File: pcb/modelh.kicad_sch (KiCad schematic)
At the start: 45 parts, among them J1 USB_C_Receptacle_USB2.0, J2 Conn_01x16, J3 Conn_01x12, J4 Conn_01x04, J5 Conn_02x03_Odd_Even, J6 Conn_02x05_Odd_Even, J7 Conn_01x05, J8 Conn_01x05, J9 Conn_01x05, SW1 SW_Push, U1 STM32F103C8Tx, U2 AMS1117-3.3, Y1 8MHz

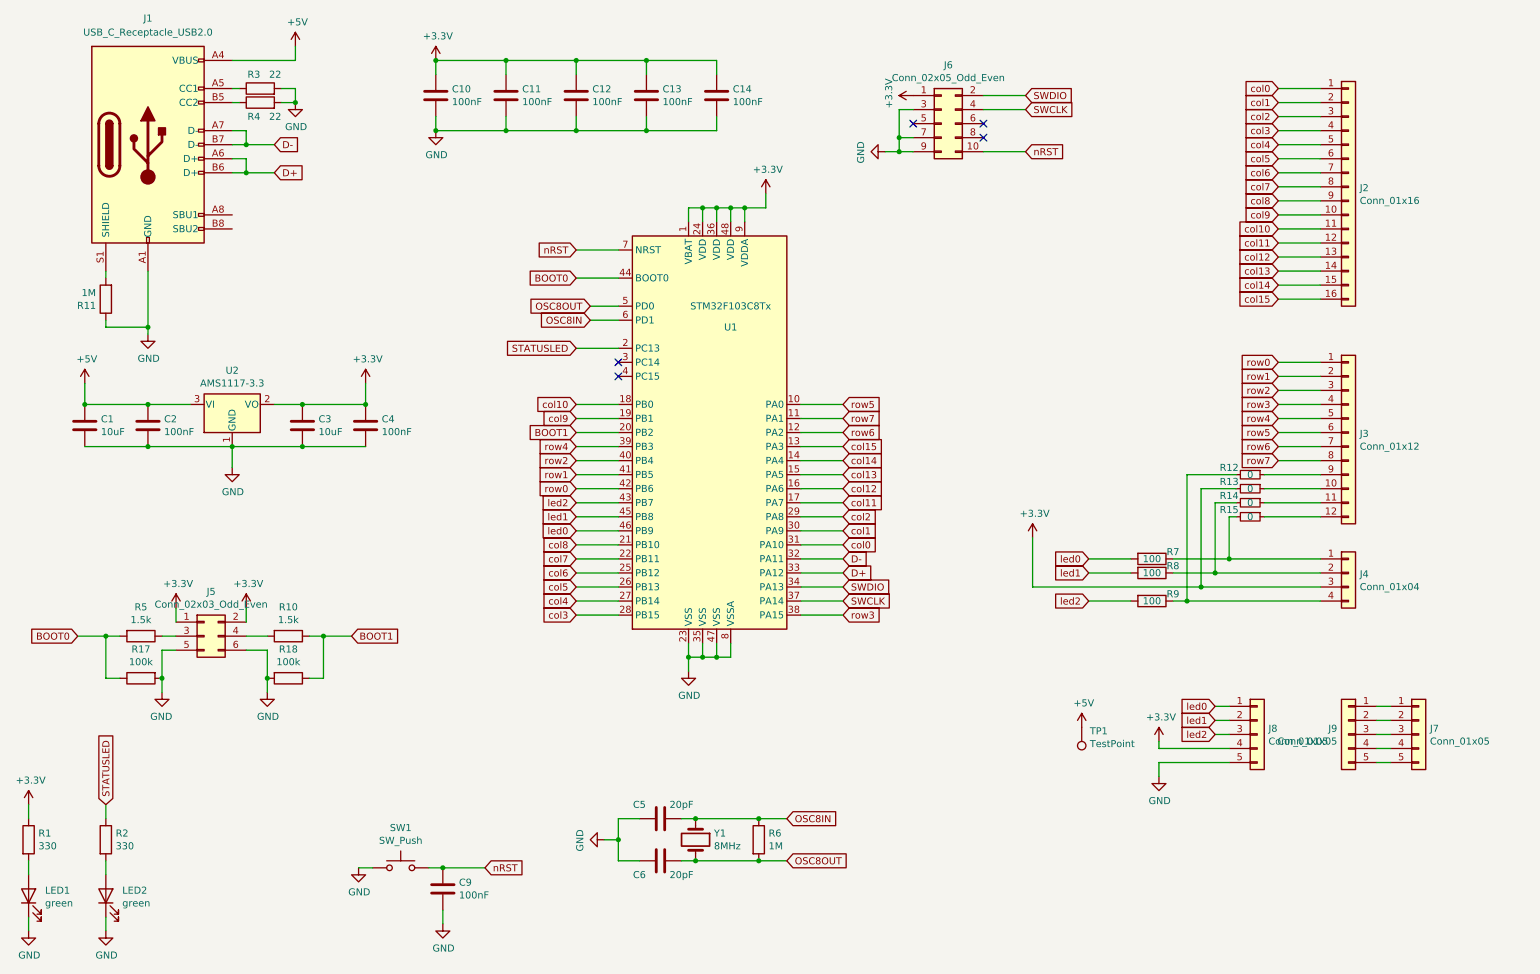
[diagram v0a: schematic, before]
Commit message: Renames a few components
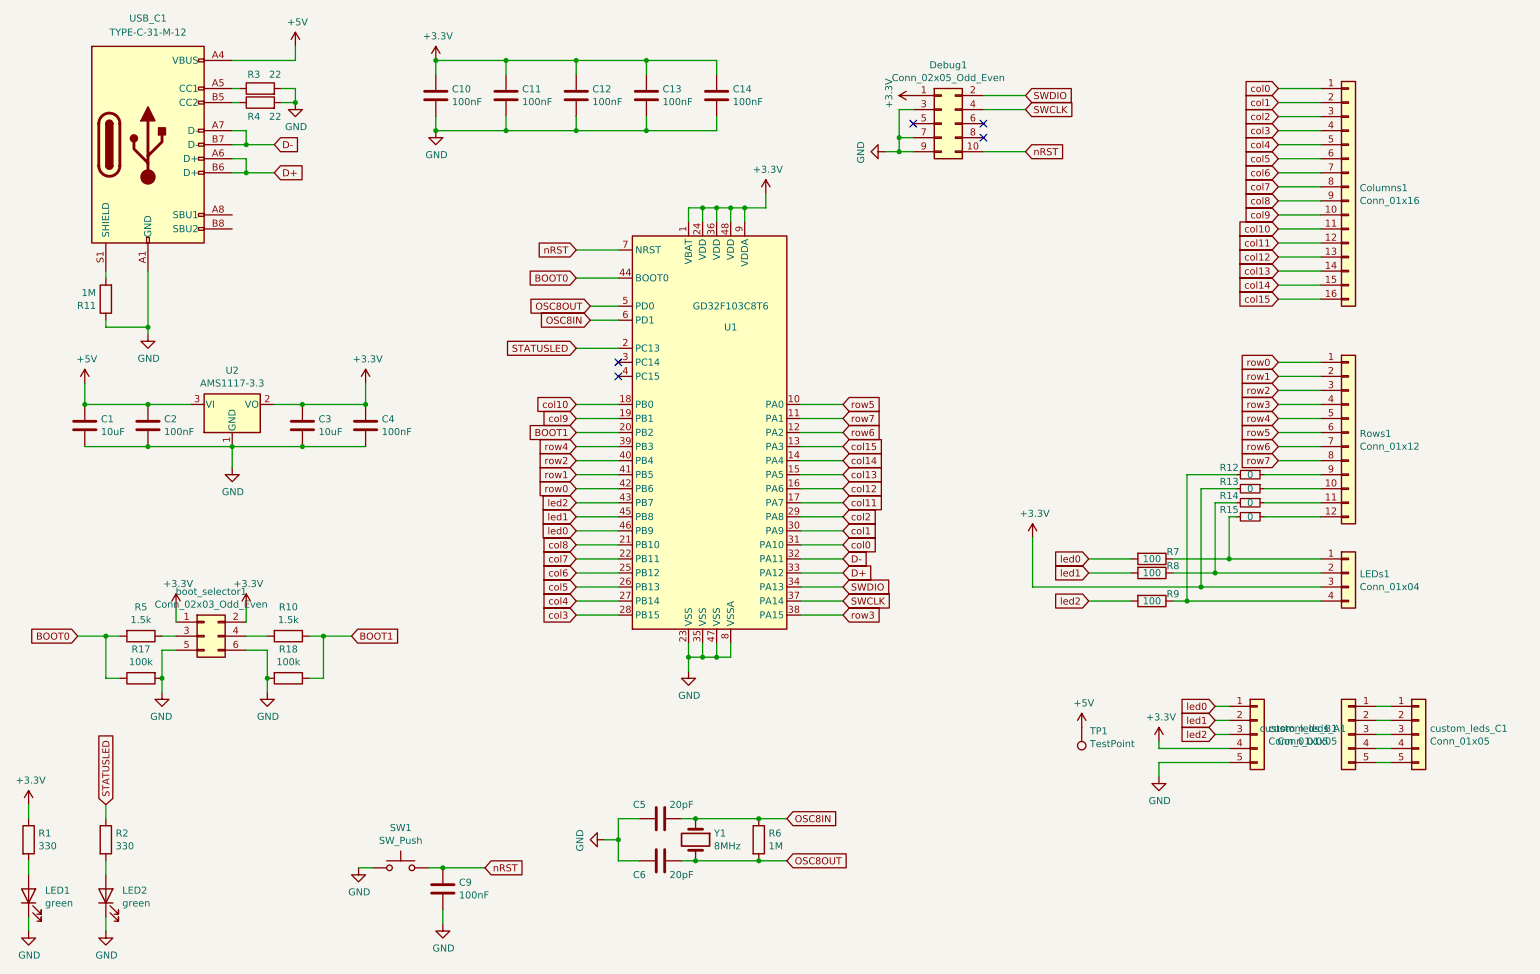
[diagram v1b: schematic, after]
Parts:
- R11: LCSC C22843 -> C269433
- U1: value STM32F103C8Tx -> GD32F103C8T6; LCSC C8734 -> C77994
- USB_C1: renamed from J1; value USB_C_Receptacle_USB2.0 -> TYPE-C-31-M-12; LCSC (none) -> C165948
- renumbered J2 to Columns1, J6 to Debug1, J4 to LEDs1, J3 to Rows1, J5 to boot_selector1, J8 to custom_leds_A1, J9 to custom_leds_B1, J7 to custom_leds_C1
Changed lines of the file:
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@@
   (symbol (lib_id "Connector_Generic:Conn_01x16") (at 261.62 49.53 0) (unit 1)
     (in_bom yes) (on_board yes)
-    (property "Reference" "J2" (id 0) (at 263.652 49.7332 0)
+    (property "Reference" "Columns1" (id 0) (at 263.652 49.7332 0)
       (effects (font (size 1.27 1.27)) (justify left))
     )
@@
   (symbol (lib_id "Connector_Generic:Conn_01x04") (at 261.62 119.38 0) (unit 1)
     (in_bom yes) (on_board yes)
-    (property "Reference" "J4" (id 0) (at 263.652 119.5832 0)
+    (property "Reference" "LEDs1" (id 0) (at 263.652 119.5832 0)
       (effects (font (size 1.27 1.27)) (justify left))
     )
@@
     (in_bom yes) (on_board yes)
     (property "Reference" "U1" (id 0) (at 149.86 74.93 0))
-    (property "Value" "STM32F103C8Tx" (id 1) (at 149.86 71.12 0))
+    (property "Value" "GD32F103C8T6" (id 1) (at 149.86 71.12 0))
     (property "Footprint" "Package_QFP:LQFP-48_7x7mm_P0.5mm" (id 2) (at 132.08 129.54 0)
       (effects (font (size 1.27 1.27)) (justify right) hide)
     )
-    (property "Datasheet" "http://www.st.com/st-web-ui/static/active/en/resource/technical/document/datasheet/CD00161566.pdf" (id 3) (at 147.32 93.98 0)
-      (effects (font (size 1.27 1.27)) hide)
-    )
-    (property "LCSC" "C8734" (id 4) (at 147.32 93.98 0)
+    (property "Datasheet" "https://datasheet.lcsc.com/lcsc/1809201023_GigaDevice-Semicon-Beijing-GD32F103C8T6_C77994.pdf" (id 3) (at 147.32 93.98 0)
+      (effects (font (size 1.27 1.27)) hide)
+    )
+    (property "LCSC" "C77994" (id 4) (at 147.32 93.98 0)
       (effects (font (size 1.27 1.27)) hide)
     )
@@
   (symbol (lib_id "Connector_Generic:Conn_02x05_Odd_Even") (at 187.96 38.1 0) (unit 1)
     (in_bom yes) (on_board yes)
-    (property "Reference" "J6" (id 0) (at 189.23 27.5082 0))
+    (property "Reference" "Debug1" (id 0) (at 189.23 27.5082 0))
     (property "Value" "Conn_02x05_Odd_Even" (id 1) (at 189.23 29.8196 0))
     (property "Footprint" "Connector_IDC:IDC-Header_2x05_P2.54mm_Vertical" (id 2) (at 187.96 38.1 0)
@@
   (symbol (lib_id "Connector_Generic:Conn_01x05") (at 274.32 148.59 0) (unit 1)
     (in_bom yes) (on_board yes)
-    (property "Reference" "J7" (id 0) (at 276.352 147.5232 0)
+    (property "Reference" "custom_leds_C1" (id 0) (at 276.352 147.5232 0)
       (effects (font (size 1.27 1.27)) (justify left))
     )
@@
   (symbol (lib_id "Connector_Generic:Conn_01x05") (at 245.11 148.59 0) (unit 1)
     (in_bom yes) (on_board yes)
-    (property "Reference" "J8" (id 0) (at 247.142 147.5232 0)
+    (property "Reference" "custom_leds_A1" (id 0) (at 247.142 147.5232 0)
       (effects (font (size 1.27 1.27)) (justify left))
     )
@@
   (symbol (lib_id "Connector_Generic:Conn_01x05") (at 261.62 148.59 0) (mirror y) (unit 1)
     (in_bom yes) (on_board yes)
-    (property "Reference" "J9" (id 0) (at 259.588 147.5232 0)
+    (property "Reference" "custom_leds_B1" (id 0) (at 259.588 147.5232 0)
       (effects (font (size 1.27 1.27)) (justify left))
     )
@@
       (effects (font (size 1.27 1.27)) hide)
     )
-    (property "LCSC" "C22843" (id 4) (at 36.83 69.85 0)
+    (property "LCSC" "C269433" (id 4) (at 36.83 69.85 0)
       (effects (font (size 1.27 1.27)) hide)
     )
@@
   (symbol (lib_id "Connector_Generic:Conn_02x03_Odd_Even") (at 54.61 130.81 0) (unit 1)
     (in_bom yes) (on_board yes)
-    (property "Reference" "J5" (id 0) (at 55.88 122.7582 0))
+    (property "Reference" "boot_selector1" (id 0) (at 55.88 122.7582 0))
     (property "Value" "Conn_02x03_Odd_Even" (id 1) (at 55.88 125.0696 0))
     (property "Footprint" "Connector_PinHeader_2.54mm:PinHeader_2x03_P2.54mm_Vertical" (id 2) (at 54.61 130.81 0)
@@
   (symbol (lib_id "Connector_Generic:Conn_01x12") (at 261.62 93.98 0) (unit 1)
     (in_bom yes) (on_board yes)
-    (property "Reference" "J3" (id 0) (at 263.652 94.1832 0)
+    (property "Reference" "Rows1" (id 0) (at 263.652 94.1832 0)
       (effects (font (size 1.27 1.27)) (justify left))
     )
@@
   (symbol (lib_id "Connector:USB_C_Receptacle_USB2.0") (at 44.45 41.91 0) (unit 1)
     (in_bom yes) (on_board yes) (fields_autoplaced)
-    (property "Reference" "J1" (id 0) (at 44.45 19.05 0))
-    (property "Value" "USB_C_Receptacle_USB2.0" (id 1) (at 44.45 21.59 0))
+    (property "Reference" "USB_C1" (id 0) (at 44.45 19.05 0))
+    (property "Value" "TYPE-C-31-M-12" (id 1) (at 44.45 21.59 0))
     (property "Footprint" "Connector_USB:USB_C_Receptacle_HRO_TYPE-C-31-M-12" (id 2) (at 48.26 41.91 0)
       (effects (font (size 1.27 1.27)) hide)
     )
     (property "Datasheet" "https://www.usb.org/sites/default/files/documents/usb_type-c.zip" (id 3) (at 48.26 41.91 0)
+      (effects (font (size 1.27 1.27)) hide)
+    )
+    (property "LCSC" "C165948" (id 4) (at 44.45 41.91 0)
       (effects (font (size 1.27 1.27)) hide)
     )
@@
       (reference "C14") (unit 1) (value "100nF") (footprint "Capacitor_SMD:C_0402_1005Metric")
     )
-    (path "/77142229-b825-44a9-8ee1-1a9eb237340e"
-      (reference "J1") (unit 1) (value "USB_C_Receptacle_USB2.0") (footprint "Connector_USB:USB_C_Receptacle_HRO_TYPE-C-31-M-12")
-    )
     (path "/00000000-0000-0000-0000-00005e88f7ea"
-      (reference "J2") (unit 1) (value "Conn_01x16") (footprint "modelh:ModelH-triomate-cols16")
-    )
-    (path "/00000000-0000-0000-0000-00005f673091"
-      (reference "J3") (unit 1) (value "Conn_01x12") (footprint "modelh:ModelH-triomate-rows12")
-    )
-    (path "/00000000-0000-0000-0000-00005e891730"
-      (reference "J4") (unit 1) (value "Conn_01x04") (footprint "modelh:ModelH-tripmate-leds4")
-    )
-    (path "/00000000-0000-0000-0000-00005f50a2de"
-      (reference "J5") (unit 1) (value "Conn_02x03_Odd_Even") (footprint "Connector_PinHeader_2.54mm:PinHeader_2x03_P2.54mm_Vertical")
+      (reference "Columns1") (unit 1) (value "Conn_01x16") (footprint "modelh:ModelH-triomate-cols16")
     )
     (path "/00000000-0000-0000-0000-00005f0cf1af"
-      (reference "J6") (unit 1) (value "Conn_02x05_Odd_Even") (footprint "Connector_IDC:IDC-Header_2x05_P2.54mm_Vertical")
-    )
-    (path "/00000000-0000-0000-0000-00005f225882"
-      (reference "J7") (unit 1) (value "Conn_01x05") (footprint "Connector_PinSocket_2.54mm:PinSocket_1x05_P2.54mm_Vertical")
-    )
-    (path "/00000000-0000-0000-0000-00005f2b29ec"
-      (reference "J8") (unit 1) (value "Conn_01x05") (footprint "Connector_PinSocket_2.54mm:PinSocket_1x05_P2.54mm_Vertical")
-    )
-    (path "/00000000-0000-0000-0000-00005f2c10c8"
-      (reference "J9") (unit 1) (value "Conn_01x05") (footprint "Connector_PinSocket_2.54mm:PinSocket_1x05_P2.54mm_Vertical")
+      (reference "Debug1") (unit 1) (value "Conn_02x05_Odd_Even") (footprint "Connector_IDC:IDC-Header_2x05_P2.54mm_Vertical")
     )
     (path "/00000000-0000-0000-0000-00005ecc1b17"
@@
       (reference "LED2") (unit 1) (value "green") (footprint "LED_SMD:LED_0805_2012Metric")
     )
+    (path "/00000000-0000-0000-0000-00005e891730"
+      (reference "LEDs1") (unit 1) (value "Conn_01x04") (footprint "modelh:ModelH-tripmate-leds4")
+    )
     (path "/00000000-0000-0000-0000-00005ecc1028"
       (reference "R1") (unit 1) (value "330") (footprint "Resistor_SMD:R_0603_1608Metric")
@@
       (reference "R18") (unit 1) (value "100k") (footprint "Resistor_SMD:R_0603_1608Metric")
     )
+    (path "/00000000-0000-0000-0000-00005f673091"
+      (reference "Rows1") (unit 1) (value "Conn_01x12") (footprint "modelh:ModelH-triomate-rows12")
+    )
     (path "/00000000-0000-0000-0000-00005ec8d26a"
       (reference "SW1") (unit 1) (value "SW_Push") (footprint "Button_Switch_SMD:SW_SPST_EVPBF")
@@
     )
     (path "/00000000-0000-0000-0000-00005f0727d7"
-      (reference "U1") (unit 1) (value "STM32F103C8Tx") (footprint "Package_QFP:LQFP-48_7x7mm_P0.5mm")
+      (reference "U1") (unit 1) (value "GD32F103C8T6") (footprint "Package_QFP:LQFP-48_7x7mm_P0.5mm")
     )
     (path "/00000000-0000-0000-0000-00005f2552b1"
       (reference "U2") (unit 1) (value "AMS1117-3.3") (footprint "Package_TO_SOT_SMD:SOT-223-3_TabPin2")
     )
+    (path "/77142229-b825-44a9-8ee1-1a9eb237340e"
+      (reference "USB_C1") (unit 1) (value "TYPE-C-31-M-12") (footprint "Connector_USB:USB_C_Receptacle_HRO_TYPE-C-31-M-12")
+    )
     (path "/00000000-0000-0000-0000-00005f127d3f"
       (reference "Y1") (unit 1) (value "8MHz") (footprint "Crystal:Crystal_SMD_5032-2Pin_5.0x3.2mm")
     )
-  )
+    (path "/00000000-0000-0000-0000-00005f50a2de"
+      (reference "boot_selector1") (unit 1) (value "Conn_02x03_Odd_Even") (footprint "Connector_PinHeader_2.54mm:PinHeader_2x03_P2.54mm_Vertical")
+    )
+    (path "/00000000-0000-0000-0000-00005f2b29ec"
+      (reference "custom_leds_A1") (unit 1) (value "Conn_01x05") (footprint "Connector_PinSocket_2.54mm:PinSocket_1x05_P2.54mm_Vertical")
+    )
+    (path "/00000000-0000-0000-0000-00005f2c10c8"
+      (reference "custom_leds_B1") (unit 1) (value "Conn_01x05") (footprint "Connector_PinSocket_2.54mm:PinSocket_1x05_P2.54mm_Vertical")
+    )
+    (path "/00000000-0000-0000-0000-00005f225882"
+      (reference "custom_leds_C1") (unit 1) (value "Conn_01x05") (footprint "Connector_PinSocket_2.54mm:PinSocket_1x05_P2.54mm_Vertical")
+    )
+  )

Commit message: Updates some components
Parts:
- R11: LCSC C269433 -> C26098
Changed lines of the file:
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@@
       (effects (font (size 1.27 1.27)) hide)
     )
-    (property "LCSC" "C269433" (id 4) (at 36.83 69.85 0)
+    (property "LCSC" " C26098" (id 4) (at 36.83 69.85 0)
       (effects (font (size 1.27 1.27)) hide)
     )

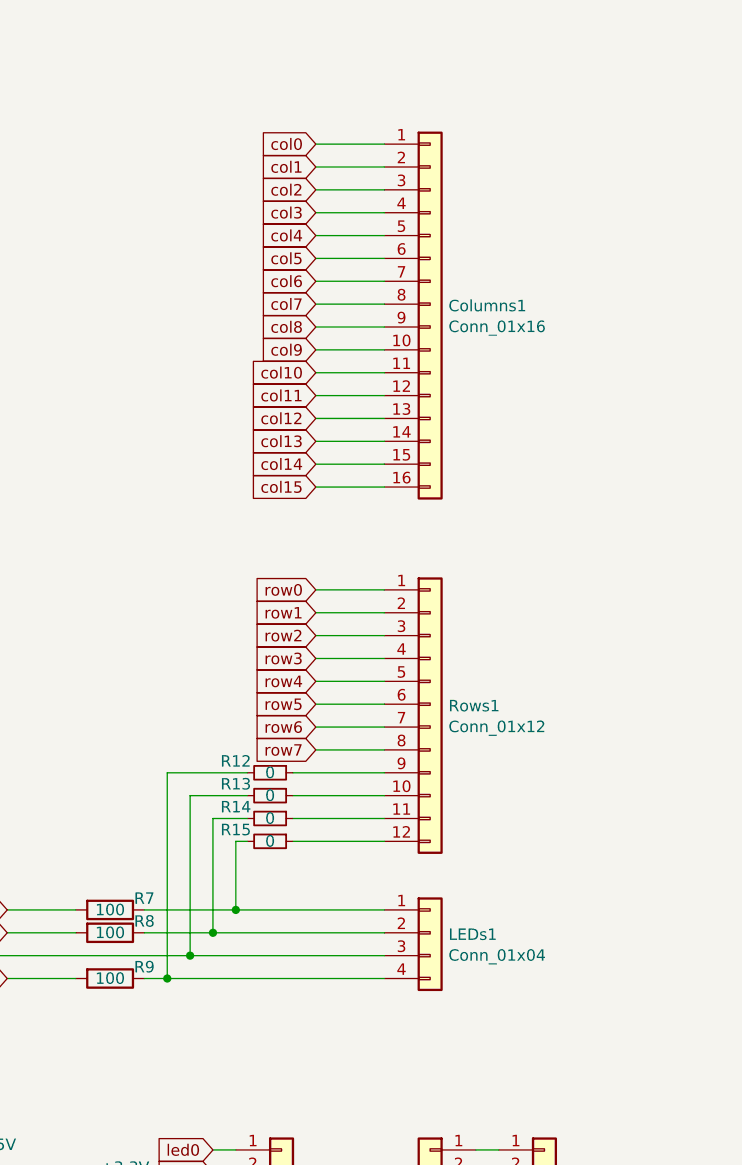
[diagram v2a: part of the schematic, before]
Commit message: Updates TE connectors footprints
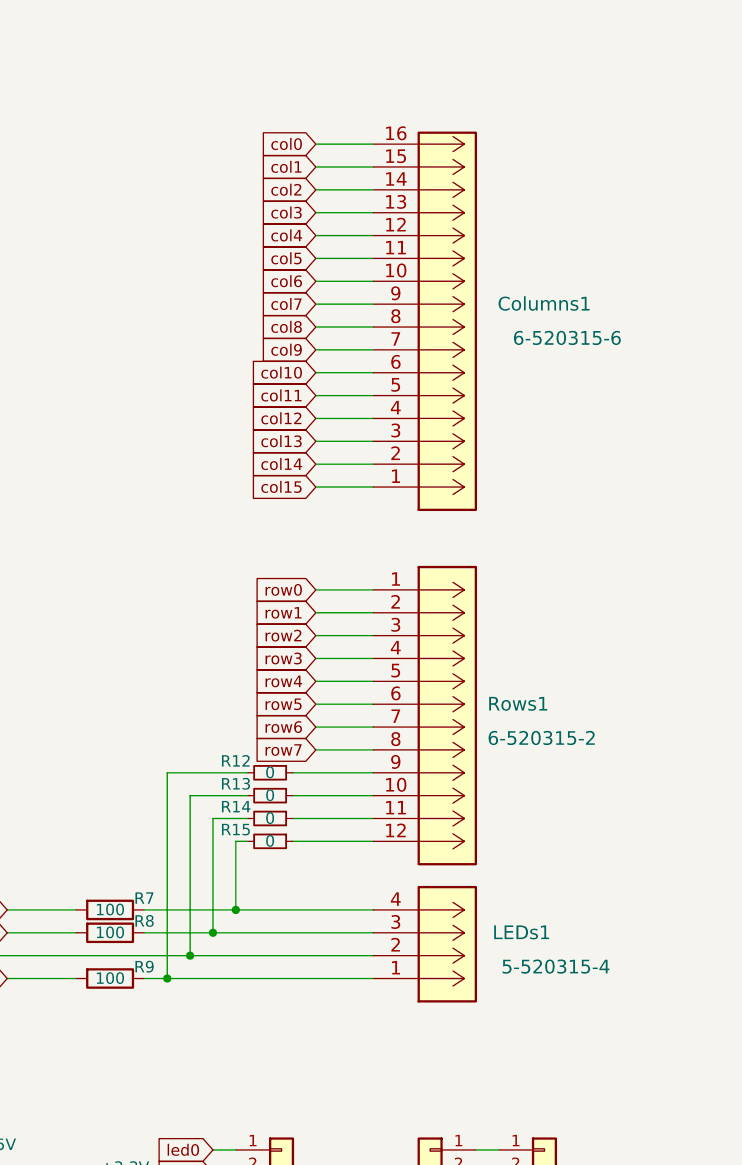
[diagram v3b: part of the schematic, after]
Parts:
- removed Columns1: Conn_01x16, modelh:ModelH-triomate-cols16, symbol Connector_Generic:Conn_01x16
- removed LEDs1: Conn_01x04, modelh:ModelH-tripmate-leds4, symbol Connector_Generic:Conn_01x04
- removed Rows1: Conn_01x12, modelh:ModelH-triomate-rows12, symbol Connector_Generic:Conn_01x12
- added Columns1: 6-520315-6, CONN_6-520315-6_TYC, symbol TE-6-520315-6:6-520315-6
- added LEDs1: 5-520315-4, CONN_5-520315-4_TYC, symbol TE-5-520315-4:5-520315-4
- added Rows1: 6-520315-2, CONN_6-520315-2_TYC, symbol TE-6-520315-2:6-520315-2
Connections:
- net +3V3: now also LEDs1.2
- net col0: now also Columns1.16
- net col1: now also Columns1.15
- net col10: now also Columns1.6
- net col11: now also Columns1.5
- net col12: now also Columns1.4
- net col13: now also Columns1.3
- net col14: now also Columns1.2
- net col15: now also Columns1.1
- net col2: now also Columns1.14
- net col3: now also Columns1.13
- net col4: now also Columns1.12
- net col5: now also Columns1.11
- net col6: now also Columns1.10
- net col7: now also Columns1.9
- net col8: now also Columns1.8
- net col9: now also Columns1.7
- net row0: now also Rows1.1
- net row1: now also Rows1.2
- net row2: now also Rows1.3
- net row3: now also Rows1.4
- net row4: now also Rows1.5
- net row5: now also Rows1.6
- net row6: now also Rows1.7
- net row7: now also Rows1.8
- net at R15.2, R7.1: now also LEDs1.4
- net at R14.2, R8.1: now also LEDs1.3
- net at R12.2, R9.1: now also LEDs1.1
- net at R13.1: now also Rows1.10
- net at R14.1: now also Rows1.11
- net at R15.1: now also Rows1.12
- net at R12.1: now also Rows1.9
